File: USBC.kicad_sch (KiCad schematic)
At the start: 4 parts, among them J2 USB_C_Receptacle_USB2.0_16P

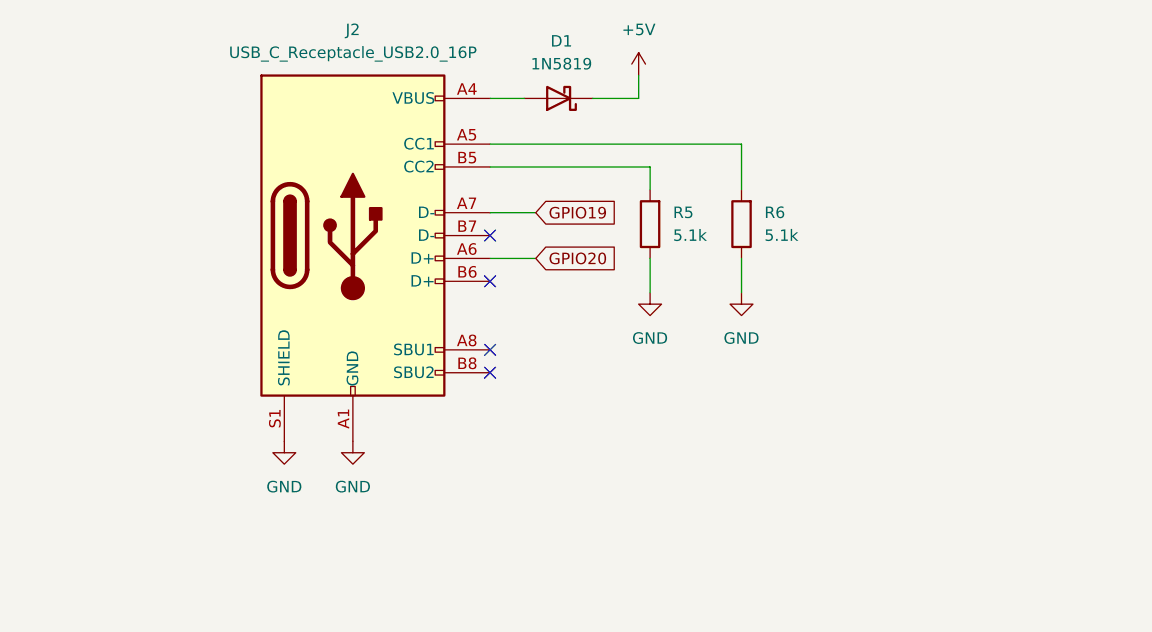
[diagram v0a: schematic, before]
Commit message: Implemented UART and an Autodownload
Added a Uart Chip and some stuff for the autodownload to make programming easier
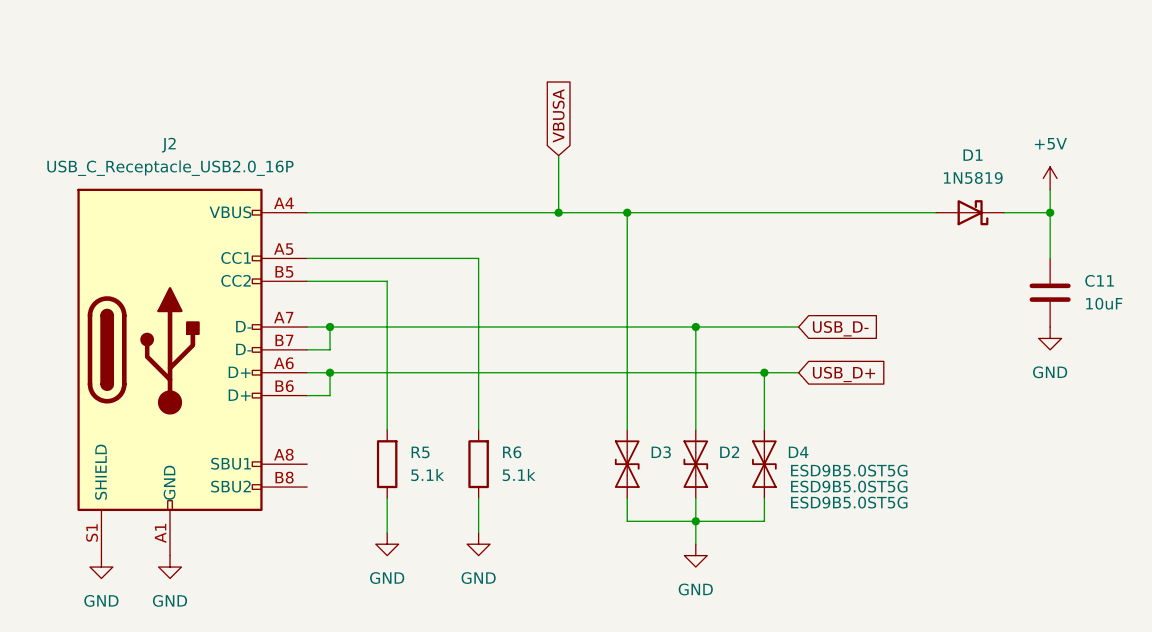
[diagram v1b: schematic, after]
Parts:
- added C11: 10uF, Capacitor_SMD:C_0603_1608Metric_Pad1.08x0.95mm_HandSolder, symbol Device:C
- added D2, D3, D4: ESD9B5.0ST5G, Diode_SMD:D_SOD-923, symbol Diode:ESD9B5.0ST5G
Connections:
- net GPIO19 is gone; now on net USB_D-: J2.A7 (D-)
- net GPIO20 is gone; now on net USB_D+: J2.A6 (D+)
- net +5V: now also C11.1
- net GND: now also C11.2, D2.1 (A1), D3.1 (A1), D4.1 (A1)
- net VBUSA: now reaches D1.2 (A), J2.A4 (VBUS), J2.A9 (VBUS), J2.B4 (VBUS), J2.B9 (VBUS)
- net VBUSA: now also D3.2 (A2)
- net USB_D+: now reaches J2.B6 (D+)
- net USB_D+: now also D4.2 (A2)
- net USB_D-: now reaches J2.B7 (D-)
- net USB_D-: now also D2.2 (A2)
- no-connect marks 4 -> 0
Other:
- moved on the sheet: D1, R5, R6

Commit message: Changed overlapping cap ref numbers
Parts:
- renumbered C11 to C23
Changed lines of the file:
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@@
 		(dnp no)
 		(fields_autoplaced yes)
-		(property "Reference" "C11"
+		(property "Reference" "C23"
 			(at 210.82 86.3599 0)
 			(effects
@@
 			(project "RFclockgen"
 				(path "/e1444a2d-a0c4-493c-a136-c624dc084e46/cc1a3e15-f832-4c98-b857-cba4ae64efa4"
-					(reference "C11")
+					(reference "C23")
 					(unit 1)
 				)
